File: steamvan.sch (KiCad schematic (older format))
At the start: 0 parts

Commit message: Update: Work on schematic
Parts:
- added C1, C2: 30p, symbol Device:C
- added C10, C11, C6: 1u, symbol Device:C
- added C3, C4, C8, C9: 100n, symbol Device:C
- added C5: 4.7u, symbol Device:C
- added C7: 10n, symbol Device:C
- added F1: 500mA, symbol Device:Polyfuse
- added J?: Conn_01x05_Male, symbol Connector:Conn_01x05_Male
- added Q1: FMMT493TA, digikey-footprints:SOT-23-3, symbol dk_Transistors-Bipolar-BJT-Single:FMMT493TA
- added RC1: 470, symbol Device:R
- added RC6, RC7: 5.1k, symbol Device:R
- added RC8: 10k, symbol Device:R
- added SW1: SW_Push, symbol Switch:SW_Push
- added U1: STM32F303CBTx, Package_QFP:LQFP-48_7x7mm_P0.5mm, symbol MCU_ST_STM32F3:STM32F303CBTx
- added U2: TLV70233_SOT23-5, Package_TO_SOT_SMD:SOT-23-5, symbol Regulator_Linear:TLV70233_SOT23-5
- added U3: NUF2221W1T2G, SOT-363, symbol NUF2221W1T2G:NUF2221W1T2G
- added USB1: HRO-TYPE-C-31-M-12, symbol Type-C:HRO-TYPE-C-31-M-12
- added Y1: 8MHz, symbol Device:Crystal_GND24
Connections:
- new net: RC8.1, SW1.2, U1.44 (BOOT0)
- new net: RC7.2, USB1.10 (CC2)
- new net: F1.2, USB1.11 (VBUS), USB1.2 (VBUS)
- new net: RC6.2, USB1.4 (CC1)
- new net: Q1.1 (B), RC1.1
- new net +3V3: C11.1, C3.1, C4.1, C5.1, C6.1, C7.1, C8.1, J?.5 (Pin_5), SW1.1, U1.1 (VBAT), U1.24 (VDD), U1.36 (VDD), U1.48 (VDD), U1.9 (VDDA), U2.5 (OUT), U3.5 (VBUS)
- new net +5V: C10.1, F1.1, U2.1 (IN), U2.3 (EN)
- new net D_N: U3.3 (D-O)
- new net D_NI: U3.4 (D-I), USB1.5 (DN2), USB1.7 (DN1)
- new net D_P: U3.1 (D+O)
- new net D_PI: U3.6 (D+I), USB1.6 (DP1), USB1.8 (DP2)
- new net GND: C1.2, C10.2, C11.2, C2.2, C3.2, C4.2, C5.2, C6.2, C7.2, C8.2, C9.2, J?.2 (Pin_2), Q1.2 (E), RC6.1, RC7.1, RC8.2, U1.23 (VSS), U1.35 (VSS), U1.47 (VSS), U1.8 (VSSA), U2.2 (GND), U3.2 (SH_GND), USB1.1 (GND), USB1.12 (GND), USB1.13 (SHIELD), Y1.2, Y1.4
- new net LEDGND: Q1.3 (C)
- new net LEDPWM: RC1.2
- new net NRST: C9.1, J?.4 (Pin_4), U1.7 (NRST)
- new net OSC_IN: C2.1, U1.5 (PF0), Y1.3
- new net OSC_OUT: C1.1, U1.6 (PF1), Y1.1
- new net SWCLK: J?.3 (Pin_3)
- new net SWDIO: J?.1 (Pin_1)
- no-connect marks 0 -> 2

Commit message: Update: Work on board schematix. Not done yet
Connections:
- net D_N: now also U1.32 (PA11)
- net D_P: now also U1.33 (PA12)
- net LEDPWM: now also U1.45 (PB8)
- net SWCLK: now also U1.37 (PA14)
- net SWDIO: now also U1.34 (PA13)
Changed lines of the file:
@@
 $Descr A4 11693 8268
 encoding utf-8
-Sheet 1 1
+Sheet 1 2
 Title ""
 Date ""
@@
 Wire Wire Line
 	7705 2740 7535 2740
+Text GLabel 7580 4140 0    50   Input ~ 0
+LEDPWM
+Wire Wire Line
+	7580 4140 7705 4140
+Text GLabel 9125 4440 2    50   Input ~ 0
+D_N
+Text GLabel 9125 4540 2    50   Input ~ 0
+D_P
+Wire Wire Line
+	9005 4440 9125 4440
+Wire Wire Line
+	9005 4540 9125 4540
+Text GLabel 9125 4640 2    50   Input ~ 0
+SWDIO
+Wire Wire Line
+	9005 4640 9125 4640
+Text GLabel 9125 4740 2    50   Input ~ 0
+SWCLK
+Wire Wire Line
+	9005 4740 9125 4740
+$Sheet
+S 4190 6305 1745 945
+U 5C226ED8
+F0 "matrix" 50
+F1 "matrix.sch" 50
+$EndSheet
 $EndSCHEMATC

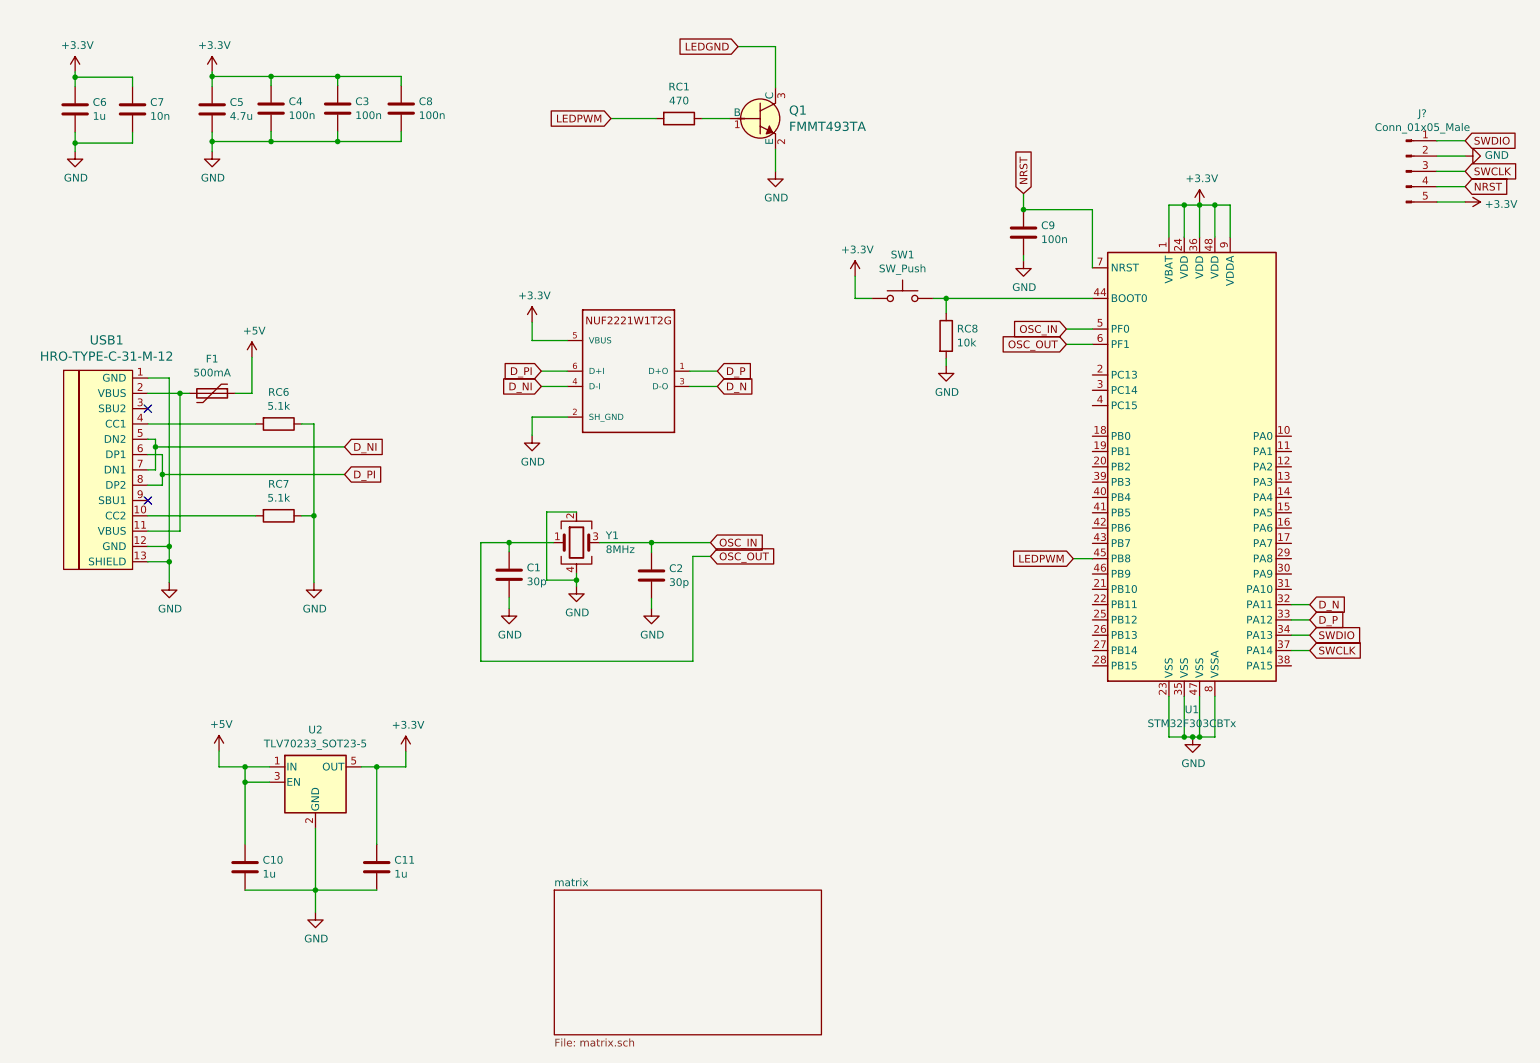
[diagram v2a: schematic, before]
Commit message: Update: Finish preliminary work on schematic
Schematic still needs review, and my pin choices for the
matrix should be double checked.
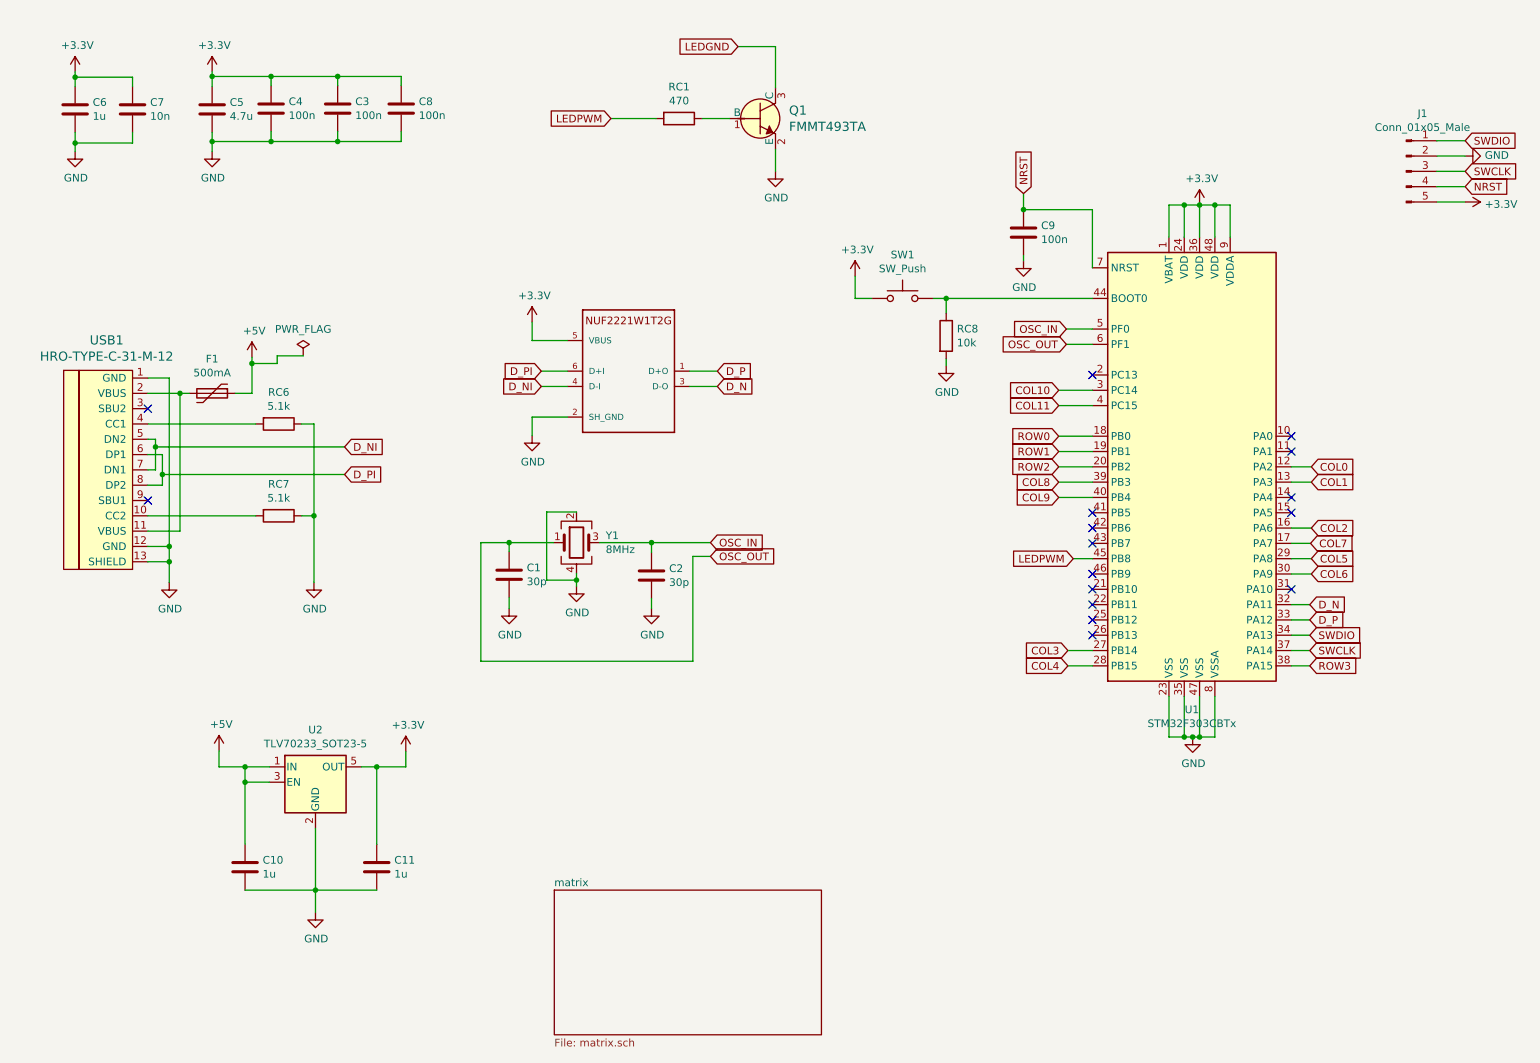
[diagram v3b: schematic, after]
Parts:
- gave numbers to parts that had none: 1
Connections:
- net COL0: now reaches U1.12 (PA2)
- net COL1: now reaches U1.13 (PA3)
- net COL2: now reaches U1.16 (PA6)
- net COL7: now reaches U1.17 (PA7)
- net ROW0: now reaches U1.18 (PB0)
- net ROW1: now reaches U1.19 (PB1)
- net ROW2: now reaches U1.20 (PB2)
- net COL3: now reaches U1.27 (PB14)
- net COL4: now reaches U1.28 (PB15)
- net COL5: now reaches U1.29 (PA8)
- net COL10: now reaches U1.3 (PC14)
- net COL6: now reaches U1.30 (PA9)
- net ROW3: now reaches U1.38 (PA15)
- net COL8: now reaches U1.39 (PB3)
- net COL11: now reaches U1.4 (PC15)
- net COL9: now reaches U1.40 (PB4)
- no-connect marks 2 -> 16
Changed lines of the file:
@@
 $EndComp
 $Comp
-L power:GND #PWR?
+L power:GND #PWR0101
 U 1 1 5C202AA6
 P 4335 4320
-F 0 "#PWR?" H 4335 4070 50  0001 C CNN
+F 0 "#PWR0101" H 4335 4070 50  0001 C CNN
 F 1 "GND" H 4340 4147 50  0000 C CNN
 F 2 "" H 4335 4320 50  0001 C CNN
@@
 	4825 4035 4825 4100
 $Comp
-L power:GND #PWR?
+L power:GND #PWR0102
 U 1 1 5C202FDA
 P 3895 4465
-F 0 "#PWR?" H 3895 4215 50  0001 C CNN
+F 0 "#PWR0102" H 3895 4215 50  0001 C CNN
 F 1 "GND" H 3900 4292 50  0000 C CNN
 F 2 "" H 3895 4465 50  0001 C CNN
@@
 $EndComp
 $Comp
-L power:GND #PWR?
+L power:GND #PWR0103
 U 1 1 5C203019
 P 4825 4465
-F 0 "#PWR?" H 4825 4215 50  0001 C CNN
+F 0 "#PWR0103" H 4825 4215 50  0001 C CNN
 F 1 "GND" H 4830 4292 50  0000 C CNN
 F 2 "" H 4825 4465 50  0001 C CNN
@@
 $EndComp
 $Comp
-L power:GND #PWR?
+L power:GND #PWR0104
 U 1 1 5C204710
 P 2630 6450
-F 0 "#PWR?" H 2630 6200 50  0001 C CNN
+F 0 "#PWR0104" H 2630 6200 50  0001 C CNN
 F 1 "GND" H 2635 6277 50  0000 C CNN
 F 2 "" H 2630 6450 50  0001 C CNN
@@
 	2630 5900 2630 6305
 $Comp
-L power:+5V #PWR?
+L power:+5V #PWR0105
 U 1 1 5C205DEA
 P 2000 5395
-F 0 "#PWR?" H 2000 5245 50  0001 C CNN
+F 0 "#PWR0105" H 2000 5245 50  0001 C CNN
 F 1 "+5V" H 2015 5568 50  0000 C CNN
 F 2 "" H 2000 5395 50  0001 C CNN
@@
 Connection ~ 2170 5500
 $Comp
-L power:+3.3V #PWR?
+L power:+3.3V #PWR0106
 U 1 1 5C206427
 P 3220 5400
-F 0 "#PWR?" H 3220 5250 50  0001 C CNN
+F 0 "#PWR0106" H 3220 5250 50  0001 C CNN
 F 1 "+3.3V" H 3235 5573 50  0000 C CNN
 F 2 "" H 3220 5400 50  0001 C CNN
@@
 $EndComp
 $Comp
-L power:+3.3V #PWR?
+L power:+3.3V #PWR0107
 U 1 1 5C2074C9
 P 4045 2595
-F 0 "#PWR?" H 4045 2445 50  0001 C CNN
+F 0 "#PWR0107" H 4045 2445 50  0001 C CNN
 F 1 "+3.3V" H 4060 2768 50  0000 C CNN
 F 2 "" H 4045 2595 50  0001 C CNN
@@
 	4045 2715 4275 2715
 $Comp
-L power:GND #PWR?
+L power:GND #PWR0108
 U 1 1 5C207BA0
 P 4045 3335
-F 0 "#PWR?" H 4045 3085 50  0001 C CNN
+F 0 "#PWR0108" H 4045 3085 50  0001 C CNN
 F 1 "GND" H 4050 3162 50  0000 C CNN
 F 2 "" H 4045 3335 50  0001 C CNN
@@
 	5635 795  5635 1065
 $Comp
-L power:GND #PWR?
+L power:GND #PWR0109
 U 1 1 5C209E46
 P 5635 1610
-F 0 "#PWR?" H 5635 1360 50  0001 C CNN
+F 0 "#PWR0109" H 5635 1360 50  0001 C CNN
 F 1 "GND" H 5640 1437 50  0000 C CNN
 F 2 "" H 5635 1610 50  0001 C CNN
@@
 	5635 1465 5635 1610
 $Comp
-L power:+3.3V #PWR?
+L power:+3.3V #PWR0110
 U 1 1 5C20B0ED
 P 1060 960
-F 0 "#PWR?" H 1060 810 50  0001 C CNN
+F 0 "#PWR0110" H 1060 810 50  0001 C CNN
 F 1 "+3.3V" H 1075 1133 50  0000 C CNN
 F 2 "" H 1060 960 50  0001 C CNN
@@
 $EndComp
 $Comp
-L power:GND #PWR?
+L power:GND #PWR0111
 U 1 1 5C20B3F2
 P 1060 1480
-F 0 "#PWR?" H 1060 1230 50  0001 C CNN
+F 0 "#PWR0111" H 1060 1230 50  0001 C CNN
 F 1 "GND" H 1065 1307 50  0000 C CNN
 F 2 "" H 1060 1480 50  0001 C CNN
@@
 	1060 1425 1060 1480
 $Comp
-L power:+3.3V #PWR?
+L power:+3.3V #PWR0112
 U 1 1 5C20DF3D
 P 1955 960
-F 0 "#PWR?" H 1955 810 50  0001 C CNN
+F 0 "#PWR0112" H 1955 810 50  0001 C CNN
 F 1 "+3.3V" H 1970 1133 50  0000 C CNN
 F 2 "" H 1955 960 50  0001 C CNN
@@
 $EndComp
 $Comp
-L power:GND #PWR?
+L power:GND #PWR0113
 U 1 1 5C20E0CB
 P 1955 1480
-F 0 "#PWR?" H 1955 1230 50  0001 C CNN
+F 0 "#PWR0113" H 1955 1230 50  0001 C CNN
 F 1 "GND" H 1960 1307 50  0000 C CNN
 F 2 "" H 1955 1480 50  0001 C CNN
@@
 	1675 4060 1535 4060
 $Comp
-L power:GND #PWR?
+L power:GND #PWR0114
 U 1 1 5C22CE88
 P 1675 4295
-F 0 "#PWR?" H 1675 4045 50  0001 C CNN
+F 0 "#PWR0114" H 1675 4045 50  0001 C CNN
 F 1 "GND" H 1680 4122 50  0000 C CNN
 F 2 "" H 1675 4295 50  0001 C CNN
@@
 	1535 3860 2240 3860
 $Comp
-L power:GND #PWR?
+L power:GND #PWR0115
 U 1 1 5C23B173
 P 2620 4295
-F 0 "#PWR?" H 2620 4045 50  0001 C CNN
+F 0 "#PWR0115" H 2620 4045 50  0001 C CNN
 F 1 "GND" H 2625 4122 50  0000 C CNN
 F 2 "" H 2620 4295 50  0001 C CNN
@@
 	2620 3860 2620 4295
 $Comp
-L Connector:Conn_01x05_Male J?
+L Connector:Conn_01x05_Male J1
 U 1 1 5C2401F1
 P 9755 1610
-F 0 "J?" H 9861 1988 50  0000 C CNN
+F 0 "J1" H 9861 1988 50  0000 C CNN
 F 1 "Conn_01x05_Male" H 9861 1897 50  0000 C CNN
 F 2 "" H 9755 1610 50  0001 C CNN
@@
 	9955 1710 10140 1710
 $Comp
-L power:GND #PWR?
+L power:GND #PWR0116
 U 1 1 5C247C97
 P 10140 1510
-F 0 "#PWR?" H 10140 1260 50  0001 C CNN
+F 0 "#PWR0116" H 10140 1260 50  0001 C CNN
 F 1 "GND" V 10145 1382 50  0000 R CNN
 F 2 "" H 10140 1510 50  0001 C CNN
@@
 $EndComp
 $Comp
-L power:+3.3V #PWR?
+L power:+3.3V #PWR0117
 U 1 1 5C247D9C
 P 10140 1810
-F 0 "#PWR?" H 10140 1660 50  0001 C CNN
+F 0 "#PWR0117" H 10140 1660 50  0001 C CNN
 F 1 "+3.3V" V 10155 1938 50  0000 L CNN
 F 2 "" H 10140 1810 50  0001 C CNN
@@
 	9955 1510 10140 1510
 $Comp
-L power:+5V #PWR?
+L power:+5V #PWR0118
 U 1 1 5C24D14C
 P 2215 2825
-F 0 "#PWR?" H 2215 2675 50  0001 C CNN
+F 0 "#PWR0118" H 2215 2675 50  0001 C CNN
 F 1 "+5V" H 2230 2998 50  0000 C CNN
 F 2 "" H 2215 2825 50  0001 C CNN
@@
 	2105 3060 2215 3060
 Wire Wire Line
-	2215 3060 2215 2825
-$Comp
-L power:+3.3V #PWR?
+	2215 3060 2215 2865
+$Comp
+L power:+3.3V #PWR0119
 U 1 1 5C2500E8
 P 8405 1830
-F 0 "#PWR?" H 8405 1680 50  0001 C CNN
+F 0 "#PWR0119" H 8405 1680 50  0001 C CNN
 F 1 "+3.3V" H 8420 2003 50  0000 C CNN
 F 2 "" H 8405 1830 50  0001 C CNN
@@
 Connection ~ 8505 1830
 $Comp
-L power:GND #PWR?
+L power:GND #PWR0120
 U 1 1 5C25E41E
 P 8360 5305
-F 0 "#PWR?" H 8360 5055 50  0001 C CNN
+F 0 "#PWR0120" H 8360 5055 50  0001 C CNN
 F 1 "GND" H 8365 5132 50  0000 C CNN
 F 2 "" H 8360 5305 50  0001 C CNN
@@
 	7705 1860 7705 2240
 $Comp
-L power:GND #PWR?
+L power:GND #PWR0121
 U 1 1 5C272EDB
 P 7255 2195
-F 0 "#PWR?" H 7255 1945 50  0001 C CNN
+F 0 "#PWR0121" H 7255 1945 50  0001 C CNN
 F 1 "GND" H 7260 2022 50  0000 C CNN
 F 2 "" H 7255 2195 50  0001 C CNN
@@
 $EndComp
 $Comp
-L power:+3.3V #PWR?
+L power:+3.3V #PWR0122
 U 1 1 5C28ED5B
 P 6155 2295
-F 0 "#PWR?" H 6155 2145 50  0001 C CNN
+F 0 "#PWR0122" H 6155 2145 50  0001 C CNN
 F 1 "+3.3V" H 6170 2468 50  0000 C CNN
 F 2 "" H 6155 2295 50  0001 C CNN
@@
 $EndComp
 $Comp
-L power:GND #PWR?
+L power:GND #PWR0123
 U 1 1 5C297829
 P 6750 2880
-F 0 "#PWR?" H 6750 2630 50  0001 C CNN
+F 0 "#PWR0123" H 6750 2630 50  0001 C CNN
 F 1 "GND" H 6755 2707 50  0000 C CNN
 F 2 "" H 6750 2880 50  0001 C CNN
@@
 F1 "matrix.sch" 50
 $EndSheet
+Text GLabel 7485 3340 0    50   Input ~ 0
+ROW0
+Text GLabel 7485 3440 0    50   Input ~ 0
+ROW1
+Text GLabel 7485 3540 0    50   Input ~ 0
+ROW2
+Wire Wire Line
+	7485 3340 7705 3340
+Wire Wire Line
+	7705 3440 7485 3440
+Wire Wire Line
+	7485 3540 7705 3540
+Text GLabel 9125 4840 2    50   Input ~ 0
+ROW3
+Wire Wire Line
+	9125 4840 9005 4840
+Text GLabel 9135 3540 2    50   Input ~ 0
+COL0
+Wire Wire Line
+	9135 3540 9005 3540
+Text GLabel 9135 3640 2    50   Input ~ 0
+COL1
+Wire Wire Line
+	9135 3640 9005 3640
+Text GLabel 9135 3940 2    50   Input ~ 0
+COL2
+Wire Wire Line
+	9005 3940 9135 3940
+Text GLabel 7545 4740 0    50   Input ~ 0
+COL3
+Text GLabel 7545 4840 0    50   Input ~ 0
+COL4
+Wire Wire Line
+	7545 4840 7705 4840
+Wire Wire Line
+	7545 4740 7705 4740
+Text GLabel 9135 4140 2    50   Input ~ 0
+COL5
+Text GLabel 9135 4240 2    50   Input ~ 0
+COL6
+Wire Wire Line
+	9005 4140 9135 4140
+Wire Wire Line
+	9005 4240 9135 4240
+Text GLabel 9130 4040 2    50   Input ~ 0
+COL7
+Wire Wire Line
+	9005 4040 9130 4040
+Text GLabel 7485 3640 0    50   Input ~ 0
+COL8
+Text GLabel 7485 3740 0    50   Input ~ 0
+COL9
+Wire Wire Line
+	7485 3640 7705 3640
+Wire Wire Line
+	7485 3740 7705 3740
+Text GLabel 7485 3040 0    50   Input ~ 0
+COL10
+Text GLabel 7485 3140 0    50   Input ~ 0
+COL11
+Wire Wire Line
+	7485 3040 7705 3040
+Wire Wire Line
+	7485 3140 7705 3140
+NoConn ~ 7705 2940
+NoConn ~ 9005 3340
+NoConn ~ 9005 3440
+NoConn ~ 9005 3740
+NoConn ~ 9005 3840
+NoConn ~ 9005 4340
+NoConn ~ 7705 4640
+NoConn ~ 7705 4540
+NoConn ~ 7705 4440
+NoConn ~ 7705 4340
+NoConn ~ 7705 4240
+NoConn ~ 7705 4040
+NoConn ~ 7705 3940
+NoConn ~ 7705 3840
+$Comp
+L power:PWR_FLAG #FLG0101
+U 1 1 5DA48319
+P 2550 2815
+F 0 "#FLG0101" H 2550 2890 50  0001 C CNN
+F 1 "PWR_FLAG" H 2550 2989 50  0000 C CNN
+F 2 "" H 2550 2815 50  0001 C CNN
+F 3 "~" H 2550 2815 50  0001 C CNN
+	1    2550 2815
+	1    0    0    -1
+$EndComp
+Wire Wire Line
+	2550 2815 2380 2815
+Wire Wire Line
+	2380 2815 2380 2865
+Wire Wire Line
+	2380 2865 2215 2865
+Connection ~ 2215 2865
+Wire Wire Line
+	2215 2865 2215 2825
 $EndSCHEMATC
